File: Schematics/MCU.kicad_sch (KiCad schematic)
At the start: 31 parts, among them J1 Microsemi_FlashPro-JTAG-10, Q3 BC817, SW1 SAMZO G4R0015010, SW2 SAMZO G4R0015010, U1 STM32F405RGT6, Y1 8mhz

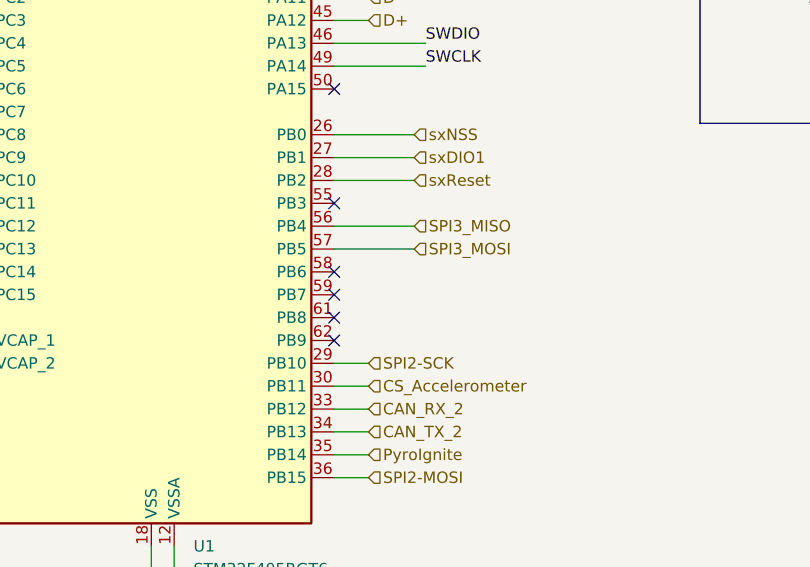
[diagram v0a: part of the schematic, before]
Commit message: added DIO0 and DIO2 pins to read lora module outputs
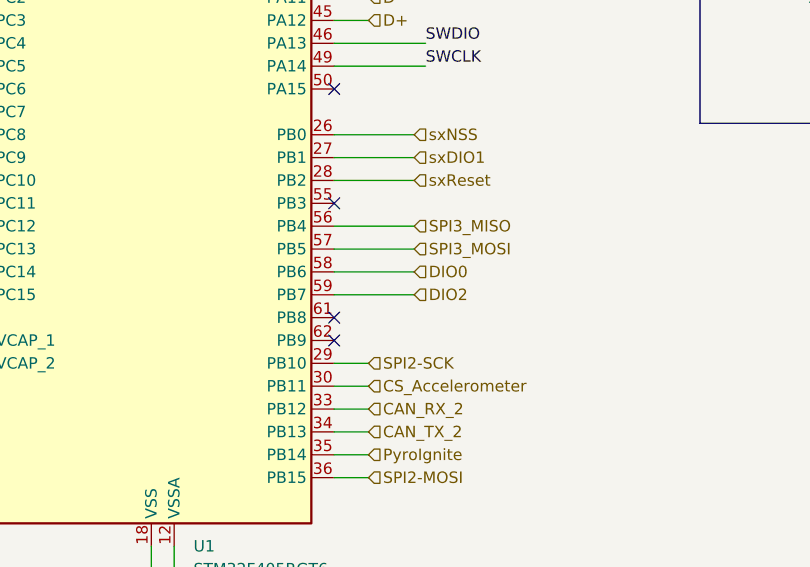
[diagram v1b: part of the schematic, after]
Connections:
- net DIO0: now reaches U1.58 (PB6)
- net DIO2: now reaches U1.59 (PB7)
- no-connect marks 20 -> 18
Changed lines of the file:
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@@
-	)
-	(no_connect
-		(at 161.29 135.89)
 	)
 	(no_connect
@@
 	)
 	(no_connect
-		(at 161.29 138.43)
-	)
-	(no_connect
 		(at 120.65 135.89)
 	)
@@
 	(wire
 		(pts
+			(xy 170.18 135.89) (xy 161.29 135.89)
+		)
+		(stroke
+			(width 0)
+			(type default)
+		)
+	)
+	(wire
+		(pts
 			(xy 165.1 97.79) (xy 161.29 97.79)
 		)
@@
 		(pts
 			(xy 119.38 44.45) (xy 130.81 44.45)
+		)
+		(stroke
+			(width 0)
+			(type default)
+		)
+	)
+	(wire
+		(pts
+			(xy 170.18 138.43) (xy 161.29 138.43)
 		)
 		(stroke
@@
 		)
 	)
+	(hierarchical_label "DIO0"
+		(shape input)
+		(at 170.18 135.89 0)
+		(effects
+			(font
+				(size 1.27 1.27)
+			)
+			(justify left)
+		)
+	)
 	(hierarchical_label "SPI2-MOSI"
 		(shape input)
@@
 		(effects
 			(font
+				(size 1.27 1.27)
+			)
+			(justify left)
+		)
+	)
+	(hierarchical_label "DIO2"
+		(shape input)
+		(at 170.18 138.43 0)
+		(effects
+			(font
